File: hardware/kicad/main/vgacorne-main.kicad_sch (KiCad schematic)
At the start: 135 parts, among them J1 TYPE-C-31-M-12, J2 SWD, J3 SM10B-SRSS-TB, J4 MCU module, SW1 C0R0, SW10 C3R0, SW11 C3R1, SW12 C3R2, SW13 C4R0, SW14 C4R1, SW15 C4R2, SW16 C5R0, SW17 C5R1, SW18 C5R2, SW19 T0, SW2 C0R1, SW20 T1, SW21 T2, SW22 BOOT, SW23 RESET, SW3 C0R2, SW4 C1R0, SW5 C1R1, SW6 C1R2, SW7 C2R0, SW8 C2R1, SW9 C2R2, U11 SN74LV4051APWR, U12 SN74LV4051APWR, U13 SN74LV4051APWR, U2 TLV75733PDBVR, U3 XC6206P332MR, U4 USBLC6-2SC6, U6 SRV05-4, U7 SRV05-4

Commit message: Add trackpad, mouse column and scroll wheel; move MCU and ports
Layout
- MCU module, USB-C and trackpad move to the right half; the left half
  is now the passive satellite.
- VGA daughterboard bay moves to the inner-back corner so both cables
  leave from the back face. The bay sits 4.5 mm further back than the
  keys need, so both halves are 116 mm deep.
- Azoteq TPS65 trackpad, landscape, right beside Y/H/N under a 1 mm
  overlay. The MCU module moves to a PCB ear behind it, next to the
  VGA bay. trackpad.py selects the pad (TPS65 or 40 mm Cirque); the
  case pocket, J5 connector and QMK driver follow the selection.
- Left half: a mouse column beside T/G/B with a scroll wheel (Bourns
  PEC12R) at the top and left/right-click HE keys beside G and B.

Circuits and firmware
- Mux channels reassigned so the satellite's mouse keys and wheel fill
  its three spare channels. The wheel's A/B contacts are summed into
  four voltage levels on one channel.
- QMK: 44-key LAYOUT and a wheel decoder that feeds QMK's quadrature
  encoder driver. Trackpad on I2C1, with rules.mk now generated. The
  host test covers the wheel.
- libhmk: MS_BTN1/MS_BTN2 on the mouse keys (no encoder support).

Case and renders
- Smoother milled case: 7.25 mm walls, 25 mm minimum outside radius
  and a flat back face at the ports.
- render.py builds Blender Cycles renders from the design geometry.

Co-Authored-By: Claude Opus 5.5 (1M context) <noreply@anthropic.com>
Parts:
- added C16: 1u, Capacitor_SMD:C_0603_1608Metric, symbol Device:C
- added C17: 100n, Capacitor_SMD:C_0402_1005Metric, symbol Device:C
- added J5: Trackpad, Connector_FFC-FPC:Jushuo_AFC07-S06FCA-00_1x6-1MP_P0.50_Horizontal, symbol Connector_Generic_MountingPin:Conn_01x06_MountingPin
- added R19, R20: 4.7k, Resistor_SMD:R_0402_1005Metric, symbol Device:R
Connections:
- net +3V3: now also C16.1, J5.4 (Pin_4), R19.2, R20.2
- net GND: now also U13.2 (A6), U13.4 (A7), U13.5 (A5), C16.2, C17.2, J5.3 (Pin_3), J5.MP (MountPin); no longer J4.1 (Pin_1), J4.2 (Pin_2), U11.2 (A6), U11.4 (A7), U12.4 (A7)
- net HE_C2R0: now also U11.2 (A6); no longer U12.13 (A0)
- net HE_C2R1: now also U11.4 (A7); no longer U12.14 (A1)
- net HE_C2R2: now also U12.13 (A0); no longer U12.15 (A2)
- net HE_C3R0: now also U12.14 (A1); no longer U12.12 (A3)
- net HE_C3R1: now also U12.15 (A2); no longer U12.1 (A4)
- net HE_C3R2: now also U12.12 (A3); no longer U12.5 (A5)
- net HE_C4R0: now also U12.1 (A4); no longer U13.13 (A0)
- net HE_C4R1: now also U12.5 (A5); no longer U13.14 (A1)
- net HE_C4R2: now also U12.2 (A6); no longer U13.15 (A2)
- net HE_C5R0: now also U13.13 (A0); no longer U13.12 (A3)
- net HE_C5R1: now also U13.14 (A1); no longer U13.1 (A4)
- net HE_C5R2: now also U13.15 (A2); no longer U13.5 (A5)
- net HE_T0: now also U12.4 (A7); no longer U12.2 (A6)
- net HE_T1: now also U13.12 (A3); no longer U13.2 (A6)
- net HE_T2: now also U13.1 (A4); no longer U13.4 (A7)
- new net I2C_SCL: J4.1 (Pin_1), J5.5 (Pin_5), R19.1
- new net I2C_SDA: J4.2 (Pin_2), J5.6 (Pin_6), R20.1
- new net TP_NRST: C17.1, J5.2 (Pin_2)
- no-connect marks 5 -> 6
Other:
- note added: "Link to the satellite half (VGA daughterboard)"
- note added: "Trackpad (optional)"
- note removed: "Link to right half (VGA daughterboard)"
- title: VGACorne - main (left) half -> VGACorne - main (right) half

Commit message: Solder the MCU module flat under the trackpad
The plug-in module stood 8 mm tall on a 2x12 socket, on a PCB ear
behind the trackpad that reached back to the rear face. That kept the
right half's back edge straight across most of the trackpad.

It is now a castellated stamp module:
- 19.4 x 25 mm, with 2x12 half-holes at 1.27 mm and every part on top.
- Soldered onto landing pads J4 on the main PCB's tab, beside Y/H/N,
  under the trackpad.
- About 2.7 mm tall: 1.6 mm below the TPS65's well, 2.2 mm below the
  Cirque's.

With the ear gone, a small PCB tongue under the pad carries its FFC
connector J5. The case back now tapers right from the keys; size and
port positions are unchanged.

- New footprints: castellated module edge and matching landing pads.
- Module boards: all parts on top; a label on the flat underside.
- checks.module_connector now compares castellated hole positions with
  landing pad centres.
- Stack-up: module height and clearance are measured against the
  trackpad well.
- Parts can opt out of the BOM (the module's edge pads are not a part).
- Docs, BOM and images regenerated.

Co-Authored-By: Claude Opus 5.5 (1M context) <noreply@anthropic.com>
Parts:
- J4: footprint Connector_PinSocket_1.27mm:PinSocket_2x12_P1.27mm_Vertical_SMD -> vgacorne:Module_Castellated_Landing_2x12_P1.27mm_19.4x25mm
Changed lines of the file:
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@@
 			)
 		)
-		(property "Footprint" "Connector_PinSocket_1.27mm:PinSocket_2x12_P1.27mm_Vertical_SMD"
+		(property "Footprint" "vgacorne:Module_Castellated_Landing_2x12_P1.27mm_19.4x25mm"
 			(at 313.69 72.39 0)
 			(effects
@@
 			)
 		)
-		(property "Description" "Socket for the swappable MCU module (2x12 1.27 mm SMD, top side)"
+		(property "Description" "Landing pads for the castellated MCU module (2x12, 1.27 mm), top side under the trackpad; the module is soldered on"
 			(at 313.69 72.39 0)
 			(effects

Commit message: Fix design audit findings
Electrical:
- Re-map the castellated module's pads so neighbours on each edge follow
  the LQFP: USB D+/D- together between grounds at the corner nearest the
  USB-C, the six ADC inputs grouped beside +3.3VA, a ground away from the
  select lines.
- Put 1k between each DRV5055 output and its 4.7n cap (TI: no capacitor
  straight on the output).
- STM32F446 module: pull PB2/BOOT1 down so BOOT reaches DFU; pull PA10 up.
- Replace the XC6206 with a second TLV75733, and the link polyfuse with a
  TPS2051C switch (soft start, current limit) so hot-plugging the satellite
  can't brown out the MCU. F1 is now 750 mA.
- USB net class 0.4/0.15 mm: ~97 ohm differential against the pour on both
  2-layer boards (was ~120).
- BOM gains a Tolerance column; part numbers for the F446 crystal.

Mechanical:
- Case foam 2 mm, leaving 0.5 mm under the bottom-side parts (the old stack
  pressed the foam into every sensor).
- USB-C overhangs the ear by 0.46 mm and the opening takes a spec-maximum
  overmould (13.95 x 8.1 mm); the old 11 x 6 mm stopped most plugs short.
- DE-15 rear-mount cutout 20.5 x 11.4 mm; floor pockets under the USB-C and
  encoder pins; plate foam clears the module and the encoder's pins.
- Knob 11.5 mm tall so it clears the encoder's collar.

Docs, PCB images and renders updated to match.

Co-Authored-By: Claude Opus 5.5 (1M context) <noreply@anthropic.com>
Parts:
- removed F2: 500mA, Fuse:Fuse_0805_2012Metric, symbol Device:Polyfuse
- added C18: 100n, Capacitor_SMD:C_0402_1005Metric, symbol Device:C
- added R301, R302, R303, R304, R305, R306, R307, R308, R309, R310, R311, R312, R313, R314, R315, R316, R317, R318, R319, R320, R321: 1k, Resistor_SMD:R_0402_1005Metric, symbol Device:R
- added U8: TPS2051CDBVR, Package_TO_SOT_SMD:SOT-23-5, symbol Power_Management:TPS2051CDBV
- F1: value 500mA -> 750mA; MPN BSMD0805-050-24V -> SMD0805-075
- U3: value XC6206P332MR -> TLV75733PDBVR; footprint Package_TO_SOT_SMD:SOT-23-3 -> Package_TO_SOT_SMD:SOT-23-5; symbol Regulator_Linear:XC6206PxxxMR -> Regulator_Linear:TLV75733PDBV; MPN XC6206P332MR-G -> TLV75733PDBVR
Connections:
- net +3.3VA: now also J4.10 (Pin_10); no longer J4.4 (Pin_4)
- net +3V3: now also J4.11 (Pin_11), U3.5 (OUT); no longer J4.3 (Pin_3), U3.2 (VO)
- net +5V: now also J4.9 (Pin_9), U3.1 (IN), C18.1, U8.4 (EN), U8.5 (IN); no longer J4.5 (Pin_5)
- net ADC_L_A: now also J4.12 (Pin_12); no longer J4.11 (Pin_11)
- net ADC_L_B: now also J4.14 (Pin_14); no longer J4.12 (Pin_12)
- net ADC_L_C: now also J4.16 (Pin_16); no longer J4.13 (Pin_13)
- net ADC_R_A: now also J4.18 (Pin_18); no longer J4.14 (Pin_14)
- net ADC_R_B: now also J4.20 (Pin_20); no longer J4.15 (Pin_15)
- net ADC_R_C: now also J4.22 (Pin_22); no longer J4.16 (Pin_16)
- net BOOT: now also J4.3 (Pin_3); no longer J4.22 (Pin_22)
- net DET: now also J4.24 (Pin_24); no longer J4.20 (Pin_20)
- net GND: now also J4.17 (Pin_17), J4.23 (Pin_23), J4.8 (Pin_8), U3.2 (GND), C18.2, U8.2 (GND); no longer J4.10 (Pin_10), J4.6 (Pin_6), J4.9 (Pin_9), U3.1 (GND)
- net HE_C0R0: now also R301.2; no longer HE1.2 (OUT)
- net HE_C0R1: now also R302.2; no longer HE2.2 (OUT)
- net HE_C0R2: now also R303.2; no longer HE3.2 (OUT)
- net HE_C1R0: now also R304.2; no longer HE4.2 (OUT)
- net HE_C1R1: now also R305.2; no longer HE5.2 (OUT)
- net HE_C1R2: now also R306.2; no longer HE6.2 (OUT)
- net HE_C2R0: now also R307.2; no longer HE7.2 (OUT)
- net HE_C2R1: now also R308.2; no longer HE8.2 (OUT)
- net HE_C2R2: now also R309.2; no longer HE9.2 (OUT)
- net HE_C3R0: now also R310.2; no longer HE10.2 (OUT)
- net HE_C3R1: now also R311.2; no longer HE11.2 (OUT)
- net HE_C3R2: now also R312.2; no longer HE12.2 (OUT)
- net HE_C4R0: now also R313.2; no longer HE13.2 (OUT)
- net HE_C4R1: now also R314.2; no longer HE14.2 (OUT)
- net HE_C4R2: now also R315.2; no longer HE15.2 (OUT)
- net HE_C5R0: now also R316.2; no longer HE16.2 (OUT)
- net HE_C5R1: now also R317.2; no longer HE17.2 (OUT)
- net HE_C5R2: now also R318.2; no longer HE18.2 (OUT)
- net HE_T0: now also R319.2; no longer HE19.2 (OUT)
- net HE_T1: now also R320.2; no longer HE20.2 (OUT)
- net HE_T2: now also R321.2; no longer HE21.2 (OUT)
- net I2C_SCL: now also J4.7 (Pin_7); no longer J4.1 (Pin_1)
- net I2C_SDA: now also J4.5 (Pin_5); no longer J4.2 (Pin_2)
- net LINK_5V_F: now also U8.1 (OUT)
- net MUX_S0: now also J4.2 (Pin_2); no longer J4.17 (Pin_17)
- net MUX_S1: now also J4.4 (Pin_4); no longer J4.18 (Pin_18)
- net MUX_S2: now also J4.6 (Pin_6); no longer J4.19 (Pin_19)
- net NRST: now also J4.1 (Pin_1); no longer J4.21 (Pin_21)
- net SWCLK: now also J4.13 (Pin_13); no longer J4.24 (Pin_24)
- net SWDIO: now also J4.15 (Pin_15); no longer J4.23 (Pin_23)
- net USB_DN: now also J4.21 (Pin_21); no longer J4.8 (Pin_8)
- net USB_DP: now also J4.19 (Pin_19); no longer J4.7 (Pin_7)
- new net HE_C0R0_OUT: HE1.2 (OUT), R301.1
- new net HE_C0R1_OUT: HE2.2 (OUT), R302.1
- new net HE_C0R2_OUT: HE3.2 (OUT), R303.1
- new net HE_C1R0_OUT: HE4.2 (OUT), R304.1
- new net HE_C1R1_OUT: HE5.2 (OUT), R305.1
- new net HE_C1R2_OUT: HE6.2 (OUT), R306.1
- new net HE_C2R0_OUT: HE7.2 (OUT), R307.1
- new net HE_C2R1_OUT: HE8.2 (OUT), R308.1
- new net HE_C2R2_OUT: HE9.2 (OUT), R309.1
- new net HE_C3R0_OUT: HE10.2 (OUT), R310.1
- new net HE_C3R1_OUT: HE11.2 (OUT), R311.1
- new net HE_C3R2_OUT: HE12.2 (OUT), R312.1
- new net HE_C4R0_OUT: HE13.2 (OUT), R313.1
- new net HE_C4R1_OUT: HE14.2 (OUT), R314.1
- new net HE_C4R2_OUT: HE15.2 (OUT), R315.1
- new net HE_C5R0_OUT: HE16.2 (OUT), R316.1
- new net HE_C5R1_OUT: HE17.2 (OUT), R317.1
- new net HE_C5R2_OUT: HE18.2 (OUT), R318.1
- new net HE_T0_OUT: HE19.2 (OUT), R319.1
- new net HE_T1_OUT: HE20.2 (OUT), R320.1
- new net HE_T2_OUT: HE21.2 (OUT), R321.1
- no-connect marks 6 -> 7
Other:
- note added: "MCU module landing pads, boot/reset, SWD"
- note removed: "MCU module socket, boot/reset, SWD"
- moved on the sheet: C102, C103, C104, C105, C106, C107, C108, C109, C110, C111, C112, C113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

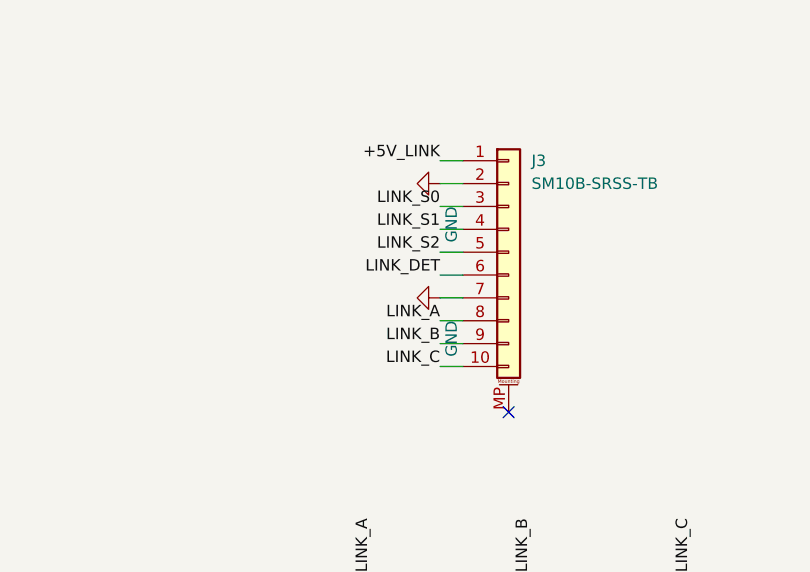
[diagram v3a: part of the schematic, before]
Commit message: Route the VGA daughterboard with Freerouting
hardware/route.py drives Freerouting directly (the KiCad MCP's autorouter
trips over a pcbnew/Python 3.14 binding bug): signals first with the
ground pours as planes, then ground as tracks round the locked signals,
then the pours and ground stitching vias. The daughterboard routes
completely and passes DRC.

To make it routable:
- the 10-pin link order now follows the DE-15 under the pigtail pads
  (J3 on both halves follows; the pigtail stays 1:1, +5 V on pin 1);
- the pigtail pads are shorter and at the board edge, leaving a via
  channel above the connector;
- the socket keeps KiCad's 1.6 mm pads round Amphenol's 1.2 mm holes,
  so a track fits between pins;
- both cable-variant jumpers sit together by pins 9 and 15.

generate.py --force pcbs now leaves boards with tracks alone.

Co-Authored-By: Claude Opus 5.5 (1M context) <noreply@anthropic.com>
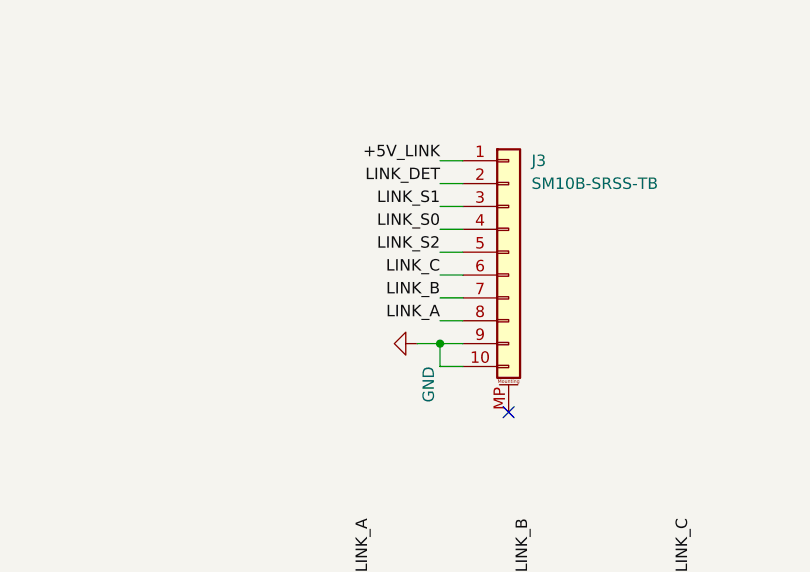
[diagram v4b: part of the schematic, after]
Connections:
- net GND: now also J3.10 (Pin_10), J3.9 (Pin_9); no longer J3.2 (Pin_2), J3.7 (Pin_7)
- net LINK_B: now also J3.7 (Pin_7); no longer J3.9 (Pin_9)
- net LINK_C: now also J3.6 (Pin_6); no longer J3.10 (Pin_10)
- net LINK_DET: now also J3.2 (Pin_2); no longer J3.6 (Pin_6)
- net LINK_S0: now also J3.4 (Pin_4); no longer J3.3 (Pin_3)
- net LINK_S1: now also J3.3 (Pin_3); no longer J3.4 (Pin_4)
